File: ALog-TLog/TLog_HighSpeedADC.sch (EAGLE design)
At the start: 95 parts, among them IC1 ATMEGA644M, J6 5.5x2.1mm Barrel, Q1 220mA/50V/3.5Ω, Q5 4.3A/20V/54mΩ, Q6 4.3A/20V/54mΩ, Q7 4.3A/20V/54mΩ, Q8 220mA/50V/3.5Ω, Q9 220mA/50V/3.5Ω, U2 FT231X-Q, U3 915MHz, U4 SX1509, X2 87832-14

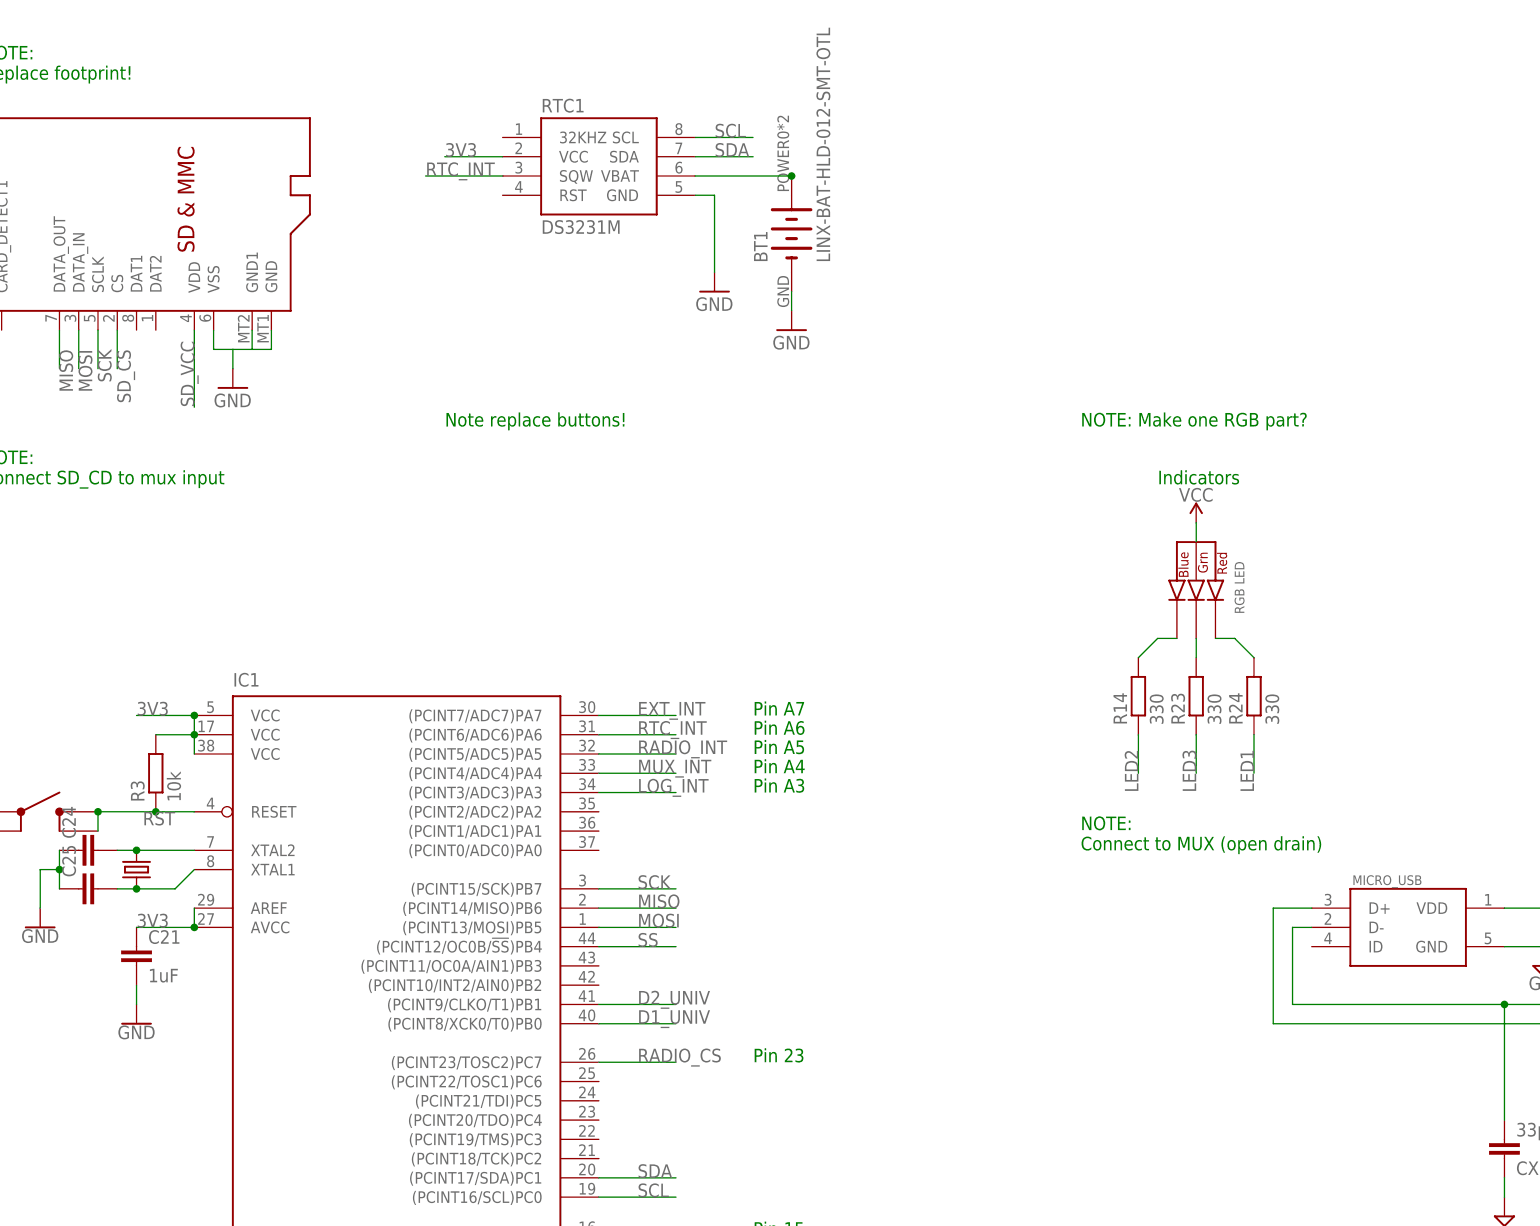
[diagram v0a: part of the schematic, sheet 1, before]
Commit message: TLog Board Ready for Review
TLog board is at functional stage and ready for review by general eyes, High Speed ADC daughter board preliminary files also added (location may change eventually)
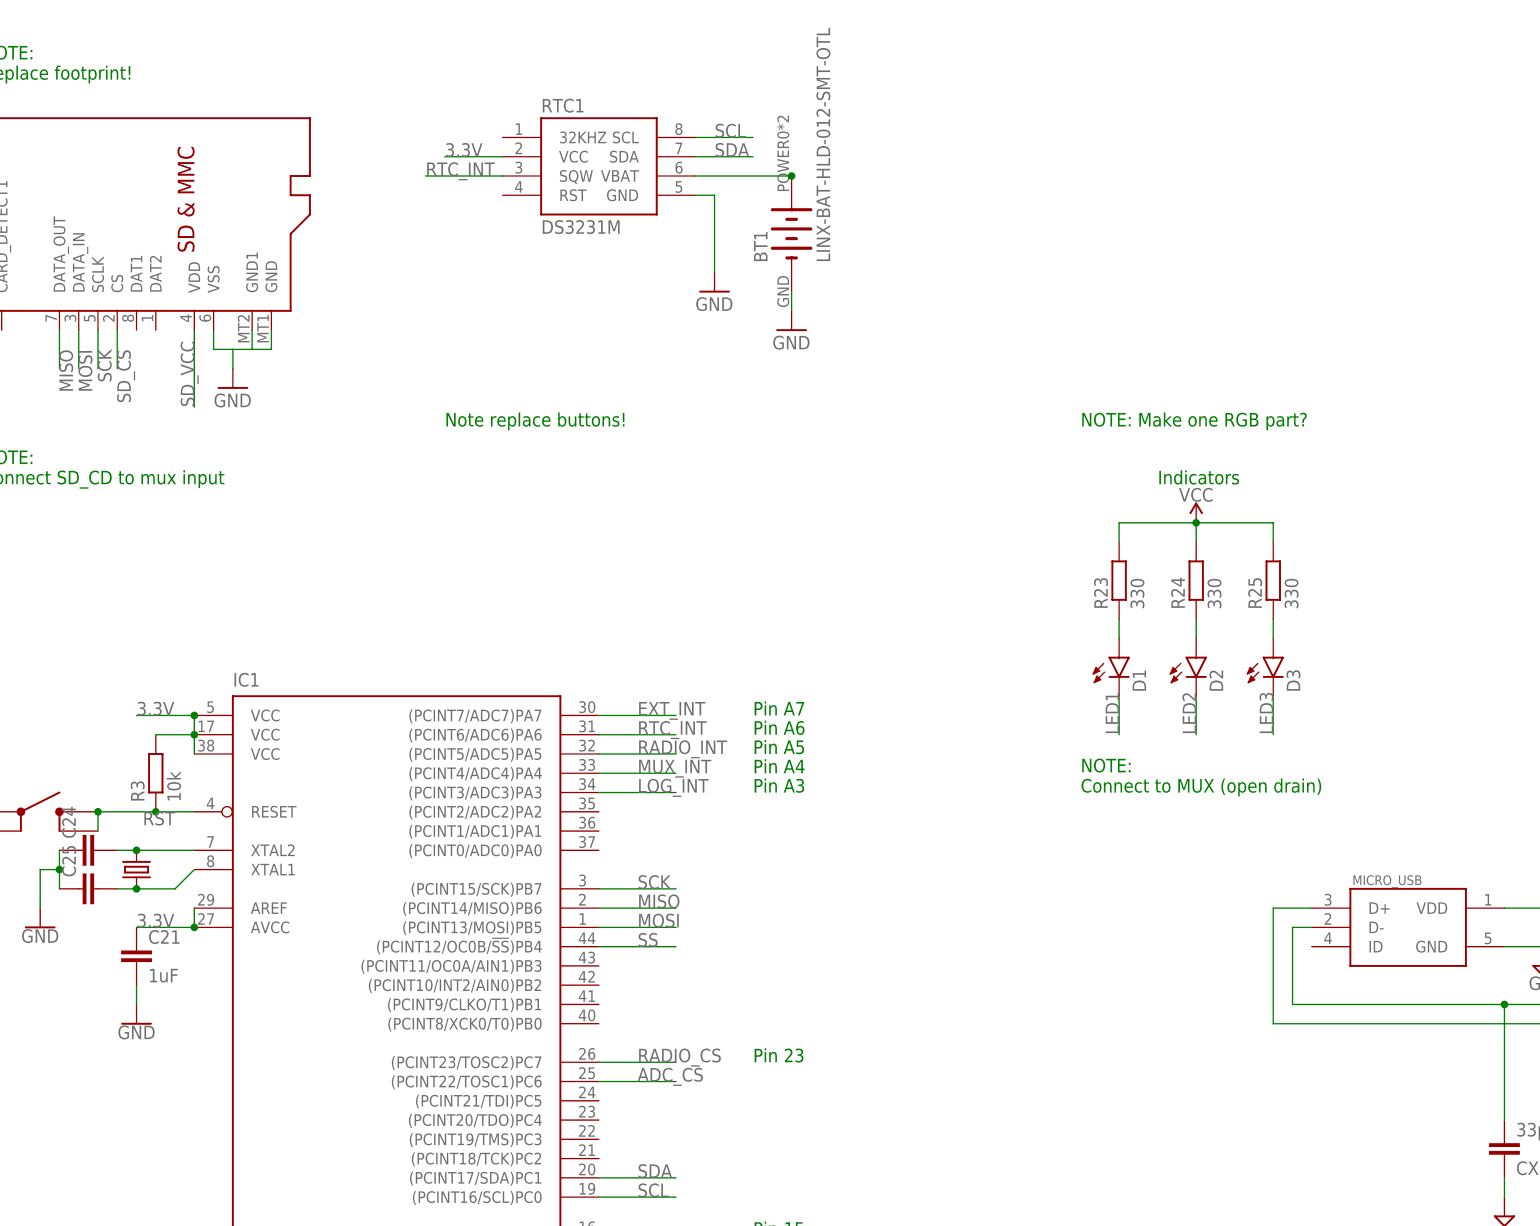
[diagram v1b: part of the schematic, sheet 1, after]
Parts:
- removed R14: 330, resistor:R-EU_R0603
- removed X2: 87832-14, con-molex:87832-14
- added D1, D2, D3: (no value), SparkFun-LED:LED0603
- added R25: 330, rcl:R-EU_R0603
- R23, R24: device resistor:R-EU_R0603 -> rcl:R-EU_R0603
- R6: value (none) -> 10k
- U$15: value CLVBA-FKA -> LTC2440; device bschulz:CLVBA-FKA -> bschulz:LTC2440
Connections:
- removed net 3V3: C10.1, C21.1, C3.1, IC1.AREF, IC1.AVCC, IC1.VCC, IC1.VCC@1, IC1.VCC@2, J1.2, J2.2, L2.P$2, Q5.S, Q7.S, Q8.G, Q9.G, R11.2, R12.2, R13.2, R3.2, R42.2, R43.2, R6.2, RTC1.VCC, U$15.ANODE, U$4.SLEEP, U$4.VOS, U$6.VCC, U$6.VCC_IO, U$6.V_BCKP, U3.3.3V, U4.VCC1, U4.VCC2, U4.VDDM, X2.2
- removed net D1_UNIV: IC1.(PCINT8/XCK0/T0)PB0, X2.5
- removed net D2_UNIV: IC1.(PCINT9/CLKO/T1)PB1
- removed net N$10: R23.2, U$15.GREEN_CATH
- removed net N$15: R24.2, U$15.RED_CATH
- removed net N$47: X2.13
- removed net N$49: X2.14
- removed net N$50: X2.12
- removed net N$9: R14.2, U$15.BLUE_CATH
- new net 3.3V: C10.1, C21.1, C3.1, IC1.AREF, IC1.AVCC, IC1.VCC, IC1.VCC@1, IC1.VCC@2, J1.2, J2.2, L2.P$2, Q1.G, Q5.S, Q7.S, Q8.G, Q9.G, R11.2, R12.2, R13.2, R23.2, R24.2, R25.2, R3.2, R42.2, R43.2, R6.2, RTC1.VCC, U$4.SLEEP, U$4.VOS, U$6.VCC, U$6.VCC_IO, U$6.V_BCKP, U3.3.3V, U4.VCC1, U4.VCC2, U4.VDDM
- new net ADC_CS: IC1.(PCINT22/TOSC1)PC6
- new net N$32: D1.A, R23.1
- new net N$33: D2.A, R24.1
- net 5V: no longer R21.1, X2.3
- net 5V_EXT_CTRL: now also Q1.S; no longer Q1.G
- net GND: now also R21.1; no longer Q1.S, X2.1
- net LED1: now also D1.C; no longer R24.1
- net LED2: now also D2.C; no longer R14.1
- net LED3: now also D3.C; no longer R23.1
- net MOSI: no longer X2.9
- net N$34: now also D3.A, R25.1; no longer X2.11
- net RX_EXT: no longer X2.7
- net SCK: no longer X2.10
- net SCL: no longer X2.6
- net SDA: no longer X2.4
- net TX_EXT: no longer X2.8
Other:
- moved on the sheet: R23, R24, R6
